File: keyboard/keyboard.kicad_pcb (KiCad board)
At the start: 2 copper layers, 214.3 x 140.5 mm, 132 parts, among them SW1 MX_SW_HS, SW10 MX_SW_HS, SW11 MX_SW_HS, SW12 MX_SW_HS, SW13 MX_SW_HS, SW14 MX_SW_HS, SW15 MX_SW_HS, SW16 MX_SW_HS, SW17 MX_SW_HS, SW18 MX_SW_HS, SW19 MX_SW_HS, SW2 MX_SW_HS, SW20 MX_SW_HS, SW21 MX_SW_HS, SW22 MX_SW_HS, SW23 MX_SW_HS, SW24 MX_SW_HS, SW25 MX_SW_HS, SW26 MX_SW_HS, SW27 MX_SW_HS, SW28 MX_SW_HS, SW29 MX_SW_HS, SW3 MX_SW_HS, SW30 MX_SW_HS, SW31 MX_SW_HS, SW32 MX_SW_HS, SW33 MX_SW_HS, SW34 MX_SW_HS, SW35 MX_SW_HS, SW36 MX_SW_HS, SW37 MX_SW_HS, SW38 MX_SW_HS, SW39 MX_SW_HS, SW4 MX_SW_HS, SW40 MX_SW_HS, SW41 MX_SW_HS, SW42 MX_SW_HS, SW43 MX_SW_HS, SW44 MX_SW_HS, SW45 MX_SW_HS, SW46 MX_SW_HS, SW47 MX_SW_HS, SW48 MX_SW_HS, SW49 MX_SW_HS, SW5 MX_SW_HS, SW50 MX_SW_HS, SW51 MX_SW_HS, SW52 MX_SW_HS, SW53 MX_SW_HS, SW54 MX_SW_HS, SW55 MX_SW_HS, SW56 MX_SW_HS, SW57 MX_SW_HS, SW58 MX_SW_HS, SW59 MX_SW_HS, SW6 MX_SW_HS, SW60 MX_SW_HS, SW61 MX_SW_HS, SW62 MX_SW_HS, SW63 MX_SW_HS, SW64 MX_SW_HS, SW7 MX_SW_HS, SW8 MX_SW_HS, SW9 MX_SW_HS, U1 ProMicro

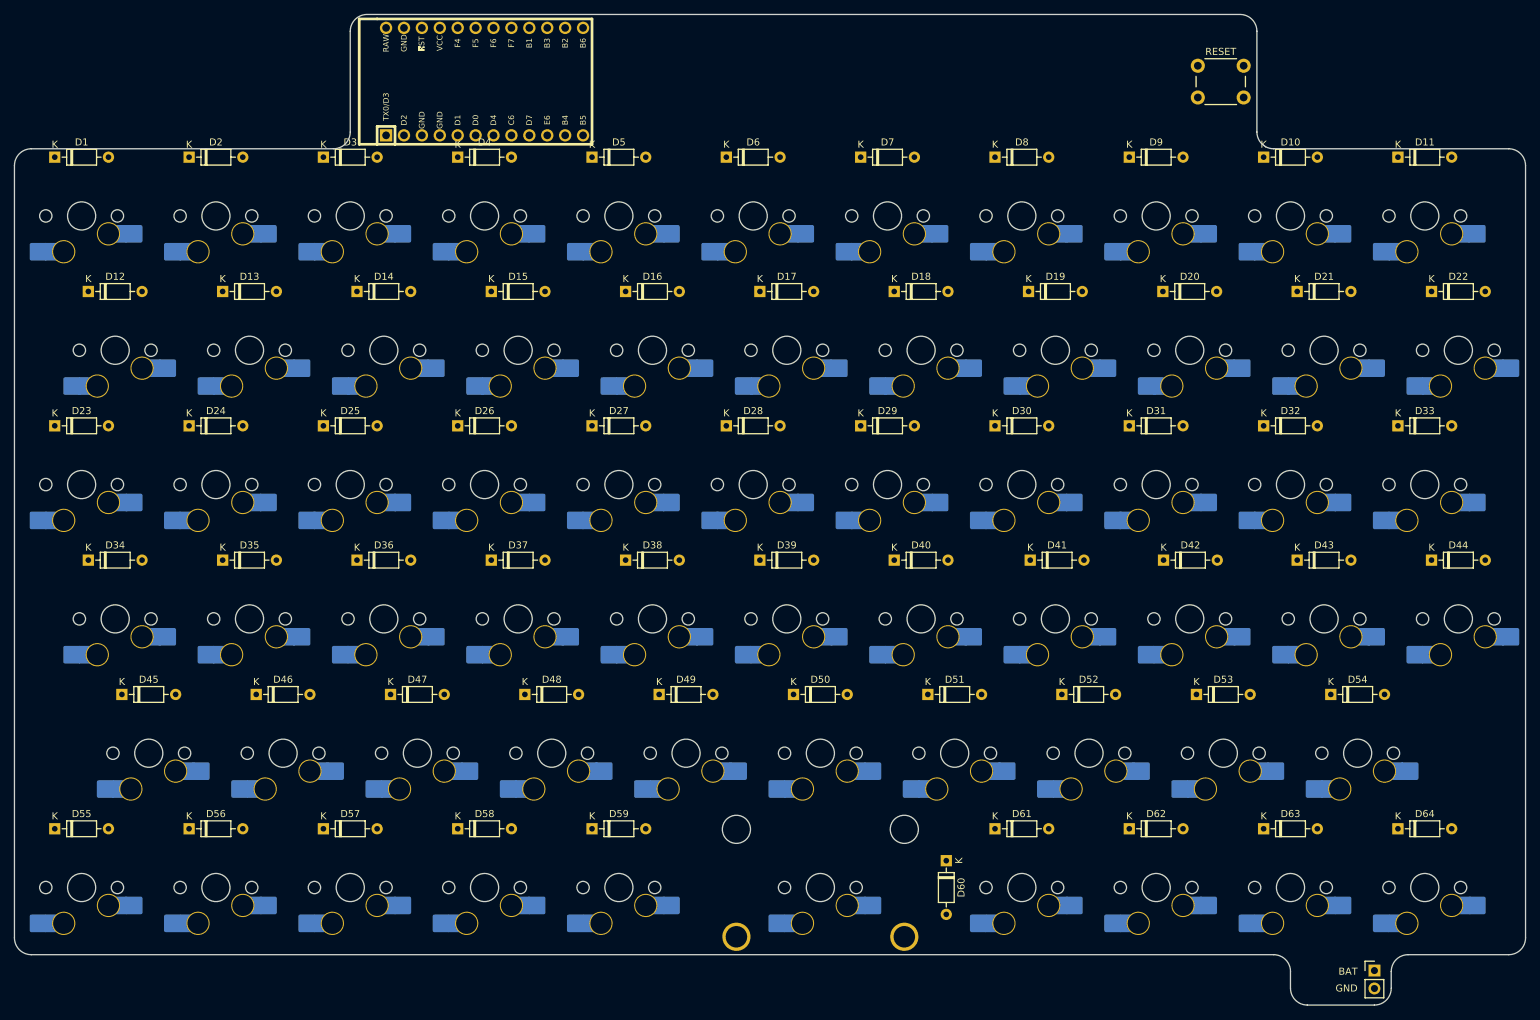
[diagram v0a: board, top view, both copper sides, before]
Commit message: Add the connector for the power switch and the holes for the broaching nuts
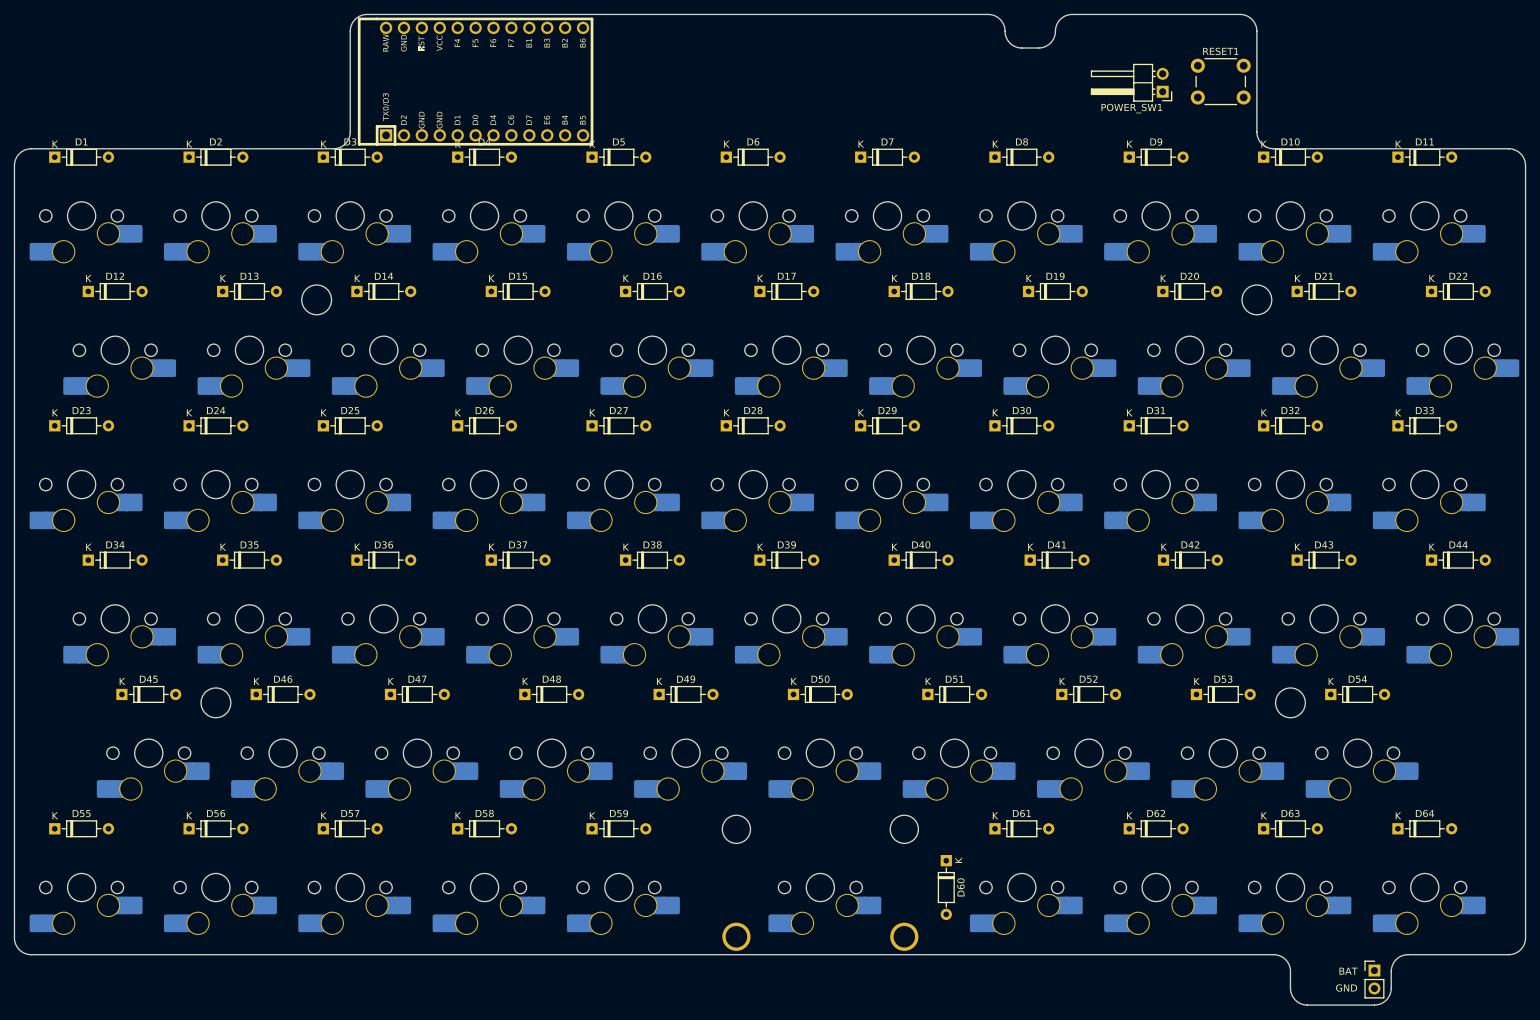
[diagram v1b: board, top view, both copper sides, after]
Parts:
- added POWER_SW1: Conn_01x02_Male, Connector_PinHeader_2.54mm:PinHeader_1x02_P2.54mm_Horizontal, F.Cu at (203.3, 25.2)
- renumbered POWER1 to BATTERY1, RESET to RESET1
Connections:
- BATTERY1 pad 1: RAW -> BAT
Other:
- outline, holes or cut-outs redrawn
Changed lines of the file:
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@@
   (net 85 "VCC")
   (net 86 "RAW")
+  (net 87 "BAT")
   (footprint "Diode_THT:D_DO-35_SOD27_P7.62mm_Horizontal" (layer "F.Cu")
     (at 184.546875 91.678125)
@@
     (property "Sheetname" "")
     (attr through_hole)
-    (fp_text reference "POWER1" (at 0 -2.33) (layer "F.SilkS") hide
+    (fp_text reference "BATTERY1" (at 0 -2.33) (layer "F.SilkS") hide
       (effects (font (size 1 1) (thickness 0.15)))
     )
@@
     (fp_line (start 1.27 -1.27) (end 1.27 3.81) (layer "F.Fab") (width 0.1))
     (pad "1" thru_hole rect (at 0 0) (size 1.7 1.7) (drill 1) (layers *.Cu *.Mask)
-      (net 86 "RAW") (pinfunction "Pin_1") (pintype "passive"))
+      (net 87 "BAT") (pinfunction "Pin_1") (pintype "passive"))
     (pad "2" thru_hole oval (at 0 2.54) (size 1.7 1.7) (drill 1) (layers *.Cu *.Mask)
       (net 81 "GND") (pinfunction "Pin_2") (pintype "passive"))
@@
     )
   )
+  (footprint "Connector_PinHeader_2.54mm:PinHeader_1x02_P2.54mm_Horizontal" (layer "F.Cu")
+    (at 203.33125 25.24875 180)
+    (descr "Through hole angled pin header, 1x02, 2.54mm pitch, 6mm pin length, single row")
+    (tags "Through hole angled pin header THT 1x02 2.54mm single row")
+    (property "Sheetfile" "keyboard.kicad_sch")
+    (property "Sheetname" "")
+    (attr through_hole)
+    (fp_text reference "POWER_SW1" (at 4.385 -2.27) (layer "F.SilkS")
+      (effects (font (size 1 1) (thickness 0.15)))
+    )
+    (fp_text value "Conn_01x02_Male" (at 4.385 4.81) (layer "F.Fab")
+      (effects (font (size 1 1) (thickness 0.15)))
+    )
+    (fp_text user "${REFERENCE}" (at 2.77 1.27 90) (layer "F.Fab")
+      (effects (font (size 1 1) (thickness 0.15)))
+    )
+    (fp_line (start 1.042929 2.92) (end 1.44 2.92) (layer "F.SilkS") (width 0.12))
+    (fp_line (start 4.1 -0.32) (end 10.1 -0.32) (layer "F.SilkS") (width 0.12))
+    (fp_line (start -1.27 -1.27) (end 0 -1.27) (layer "F.SilkS") (width 0.12))
+    (fp_line (start -1.27 0) (end -1.27 -1.27) (layer "F.SilkS") (width 0.12))
+    (fp_line (start 4.1 -0.08) (end 10.1 -0.08) (layer "F.SilkS") (width 0.12))
+    (fp_line (start 10.1 2.92) (end 4.1 2.92) (layer "F.SilkS") (width 0.12))
+    (fp_line (start 4.1 -1.33) (end 1.44 -1.33) (layer "F.SilkS") (width 0.12))
+    (fp_line (start 4.1 3.87) (end 4.1 -1.33) (layer "F.SilkS") (width 0.12))
+    (fp_line (start 1.11 -0.38) (end 1.44 -0.38) (layer "F.SilkS") (width 0.12))
+    (fp_line (start 1.44 3.87) (end 4.1 3.87) (layer "F.SilkS") (width 0.12))
+    (fp_line (start 10.1 0.38) (end 4.1 0.38) (layer "F.SilkS") (width 0.12))
+    (fp_line (start 4.1 -0.2) (end 10.1 -0.2) (layer "F.SilkS") (width 0.12))
+    (fp_line (start 4.1 0.28) (end 10.1 0.28) (layer "F.SilkS") (width 0.12))
+    (fp_line (start 4.1 -0.38) (end 10.1 -0.38) (layer "F.SilkS") (width 0.12))
+    (fp_line (start 1.44 1.27) (end 4.1 1.27) (layer "F.SilkS") (width 0.12))
+    (fp_line (start 4.1 2.16) (end 10.1 2.16) (layer "F.SilkS") (width 0.12))
+    (fp_line (start 4.1 0.16) (end 10.1 0.16) (layer "F.SilkS") (width 0.12))
+    (fp_line (start 4.1 0.04) (end 10.1 0.04) (layer "F.SilkS") (width 0.12))
+    (fp_line (start 1.042929 2.16) (end 1.44 2.16) (layer "F.SilkS") (width 0.12))
+    (fp_line (start 1.44 -1.33) (end 1.44 3.87) (layer "F.SilkS") (width 0.12))
+    (fp_line (start 1.11 0.38) (end 1.44 0.38) (layer "F.SilkS") (width 0.12))
+    (fp_line (start 10.1 -0.38) (end 10.1 0.38) (layer "F.SilkS") (width 0.12))
+    (fp_line (start 10.1 2.16) (end 10.1 2.92) (layer "F.SilkS") (width 0.12))
+    (fp_line (start 10.55 4.35) (end 10.55 -1.8) (layer "F.CrtYd") (width 0.05))
+    (fp_line (start -1.8 4.35) (end 10.55 4.35) (layer "F.CrtYd") (width 0.05))
+    (fp_line (start -1.8 -1.8) (end -1.8 4.35) (layer "F.CrtYd") (width 0.05))
+    (fp_line (start 10.55 -1.8) (end -1.8 -1.8) (layer "F.CrtYd") (width 0.05))
+    (fp_line (start 4.04 0.32) (end 10.04 0.32) (layer "F.Fab") (width 0.1))
+    (fp_line (start -0.32 -0.32) (end 1.5 -0.32) (layer "F.Fab") (width 0.1))
+    (fp_line (start -0.32 2.86) (end 1.5 2.86) (layer "F.Fab") (width 0.1))
+    (fp_line (start 1.5 3.81) (end 1.5 -0.635) (layer "F.Fab") (width 0.1))
+    (fp_line (start -0.32 -0.32) (end -0.32 0.32) (layer "F.Fab") (width 0.1))
+    (fp_line (start 10.04 2.22) (end 10.04 2.86) (layer "F.Fab") (width 0.1))
+    (fp_line (start 4.04 3.81) (end 1.5 3.81) (layer "F.Fab") (width 0.1))
+    (fp_line (start -0.32 2.22) (end -0.32 2.86) (layer "F.Fab") (width 0.1))
+    (fp_line (start 2.135 -1.27) (end 4.04 -1.27) (layer "F.Fab") (width 0.1))
+    (fp_line (start 4.04 -1.27) (end 4.04 3.81) (layer "F.Fab") (width 0.1))
+    (fp_line (start 10.04 -0.32) (end 10.04 0.32) (layer "F.Fab") (width 0.1))
+    (fp_line (start 4.04 2.86) (end 10.04 2.86) (layer "F.Fab") (width 0.1))
+    (fp_line (start 4.04 -0.32) (end 10.04 -0.32) (layer "F.Fab") (width 0.1))
+    (fp_line (start 4.04 2.22) (end 10.04 2.22) (layer "F.Fab") (width 0.1))
+    (fp_line (start 1.5 -0.635) (end 2.135 -1.27) (layer "F.Fab") (width 0.1))
+    (fp_line (start -0.32 2.22) (end 1.5 2.22) (layer "F.Fab") (width 0.1))
+    (fp_line (start -0.32 0.32) (end 1.5 0.32) (layer "F.Fab") (width 0.1))
+    (pad "1" thru_hole rect (at 0 0 180) (size 1.7 1.7) (drill 1) (layers *.Cu *.Mask)
+      (net 87 "BAT") (pinfunction "Pin_1") (pintype "passive"))
+    (pad "2" thru_hole oval (at 0 2.54 180) (size 1.7 1.7) (drill 1) (layers *.Cu *.Mask)
+      (net 86 "RAW") (pinfunction "Pin_2") (pintype "passive"))
+    (model "${KICAD6_3DMODEL_DIR}/Connector_PinHeader_2.54mm.3dshapes/PinHeader_1x02_P2.54mm_Horizontal.wrl"
+      (offset (xyz 0 0 0))
+      (scale (xyz 1 1 1))
+      (rotate (xyz 0 0 0))
+    )
+  )
   (footprint "Diode_THT:D_DO-35_SOD27_P7.62mm_Horizontal" (layer "F.Cu")
     (at 227.17125 110.728125)
@@
     (property "Sheetname" "")
     (attr through_hole)
-    (fp_text reference "RESET" (at 3.25 -2) (layer "F.SilkS")
+    (fp_text reference "RESET1" (at 3.25 -2) (layer "F.SilkS")
       (effects (font (size 1 1) (thickness 0.15)))
     )
@@
   )
   (gr_line (start 40.48125 35.71875) (end 40.48125 145.25625) (layer "Edge.Cuts") (width 0.1))
+  (gr_circle (center 216.69375 54.76875) (end 218.80375 54.76875) (layer "Edge.Cuts") (width 0.1) (fill none))
   (gr_arc (start 88.10625 30.95625) (mid 87.408798 32.640048) (end 85.725 33.3375) (layer "Edge.Cuts") (width 0.1))
+  (gr_circle (center 83.34375 54.76875) (end 85.45375 54.76875) (layer "Edge.Cuts") (width 0.1) (fill none))
   (gr_line (start 216.69375 30.95625) (end 216.69375 16.66875) (layer "Edge.Cuts") (width 0.1))
+  (gr_circle (center 221.45625 111.91875) (end 223.56625 111.91875) (layer "Edge.Cuts") (width 0.1) (fill none))
   (gr_line (start 252.4125 147.6375) (end 238.125 147.6375) (layer "Edge.Cuts") (width 0.1))
   (gr_arc (start 235.74375 150.01875) (mid 236.441202 148.334952) (end 238.125 147.6375) (layer "Edge.Cuts") (width 0.1))
   (gr_line (start 254.79375 145.25625) (end 254.79375 35.71875) (layer "Edge.Cuts") (width 0.1))
   (gr_line (start 233.3625 154.78125) (end 223.8375 154.78125) (layer "Edge.Cuts") (width 0.1))
+  (gr_arc (start 188.11875 16.66875) (mid 188.816202 14.984952) (end 190.5 14.2875) (layer "Edge.Cuts") (width 0.1))
   (gr_arc (start 252.4125 33.3375) (mid 254.096269 34.034981) (end 254.79375 35.71875) (layer "Edge.Cuts") (width 0.1))
+  (gr_arc (start 178.59375 14.2875) (mid 180.277548 14.984952) (end 180.975 16.66875) (layer "Edge.Cuts") (width 0.1))
+  (gr_circle (center 69.05625 111.91875) (end 71.16625 111.91875) (layer "Edge.Cuts") (width 0.1) (fill none))
   (gr_line (start 42.8625 147.6375) (end 219.075 147.6375) (layer "Edge.Cuts") (width 0.1))
   (gr_arc (start 235.74375 152.4) (mid 235.046298 154.083798) (end 233.3625 154.78125) (layer "Edge.Cuts") (width 0.1))
   (gr_arc (start 254.79375 145.25625) (mid 254.096269 146.940019) (end 252.4125 147.6375) (layer "Edge.Cuts") (width 0.1))
   (gr_arc (start 40.48125 35.71875) (mid 41.178717 34.034967) (end 42.8625 33.3375) (layer "Edge.Cuts") (width 0.1))
-  (gr_line (start 214.3125 14.2875) (end 90.4875 14.2875) (layer "Edge.Cuts") (width 0.1))
+  (gr_line (start 178.59375 14.2875) (end 90.4875 14.2875) (layer "Edge.Cuts") (width 0.1))
   (gr_arc (start 88.10625 16.66875) (mid 88.803702 14.984952) (end 90.4875 14.2875) (layer "Edge.Cuts") (width 0.1))
   (gr_line (start 88.10625 30.95625) (end 88.10625 16.66875) (layer "Edge.Cuts") (width 0.1))
@@
   (gr_arc (start 214.3125 14.2875) (mid 215.996298 14.984952) (end 216.69375 16.66875) (layer "Edge.Cuts") (width 0.1))
   (gr_arc (start 223.8375 154.78125) (mid 222.153702 154.083798) (end 221.45625 152.4) (layer "Edge.Cuts") (width 0.1))
+  (gr_arc (start 183.35625 19.05) (mid 181.672452 18.352548) (end 180.975 16.66875) (layer "Edge.Cuts") (width 0.1))
+  (gr_line (start 185.7375 19.05) (end 183.35625 19.05) (layer "Edge.Cuts") (width 0.1))
   (gr_line (start 221.45625 152.4) (end 221.45625 150.01875) (layer "Edge.Cuts") (width 0.1))
+  (gr_arc (start 188.11875 16.66875) (mid 187.421298 18.352548) (end 185.7375 19.05) (layer "Edge.Cuts") (width 0.1))
   (gr_arc (start 42.8625 147.6375) (mid 41.178731 146.940019) (end 40.48125 145.25625) (layer "Edge.Cuts") (width 0.1))
   (gr_arc (start 219.075 147.6375) (mid 220.758798 148.334952) (end 221.45625 150.01875) (layer "Edge.Cuts") (width 0.1))
   (gr_line (start 235.74375 150.01875) (end 235.74375 152.4) (layer "Edge.Cuts") (width 0.1))
+  (gr_line (start 190.5 14.2875) (end 214.3125 14.2875) (layer "Edge.Cuts") (width 0.1))
   (gr_arc (start 219.075 33.3375) (mid 217.391202 32.640048) (end 216.69375 30.95625) (layer "Edge.Cuts") (width 0.1))
   (gr_line (start 219.075 33.3375) (end 252.4125 33.3375) (layer "Edge.Cuts") (width 0.1))
